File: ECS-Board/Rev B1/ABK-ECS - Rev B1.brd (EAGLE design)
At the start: 100 x 100 mm, 272 parts, among them J1 USB-B-S-RA, J10 FTSH-105-01-L-DV-NOPASTE, J11 22-05-7028-02, J12 RB1-125BAG1A, J2 MSTBA2, J3 22-05-7068-06, J4 22-05-7028-02, J5 22-05-7068-06, J6 22-05-7068-06, J7 22-05-7068-06, J8 22-05-7028-02, J9 FTSH-103-01-L-DV-NOPASTE, K1 G6K-2G-Y, SW1 B3FS-1015, SW2 B3FS-1015, T1 MMBT2907ALT3, T10 MMBT2222AL, T11 IRLML5103TRPBF, T12 MMBT2222AL, T13 IRLML5103TRPBF, T14 IRLML5103TRPBF, T15 IRLML5103TRPBF, T16 IRLML5103TRPBF, T17 MMBT2222AL, T18 MMBT2222AL, T19 MMBT2222AL, T2 EXMACHINA-LOGO-NAME, T20 MMBT2222AL, T3 IRLML5103TRPBF, T4 IRLML5103TRPBF, T5 IRLML5103TRPBF, T6 IRLML5103TRPBF, T7 MMBT2222AL, T8 MMBT2222AL, T9 MMBT2222AL, U1 AT24C512C-SSHM-B, U2 LPC1768FBD100, U3 LT3686HDDPBF, U4 LT3686HDDPBF, U5 CD4050BD, U6 CD4050BD, U7 DP83848JSQ/NOPB, X1 FC-135, X2 ASE-12, X3 3000, X4 ASE_50

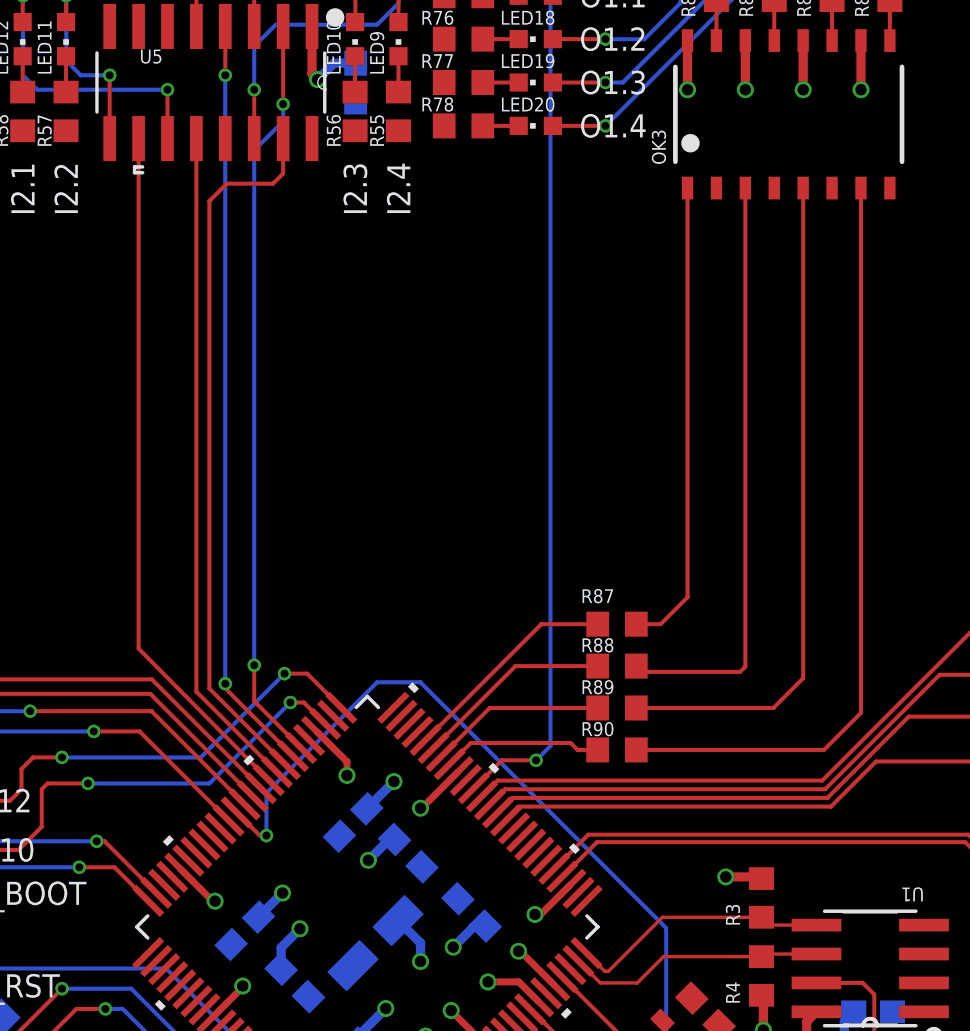
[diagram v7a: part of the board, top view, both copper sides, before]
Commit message: Remape I/O and add UART-I2C-2ADC-Encoder mcu pin
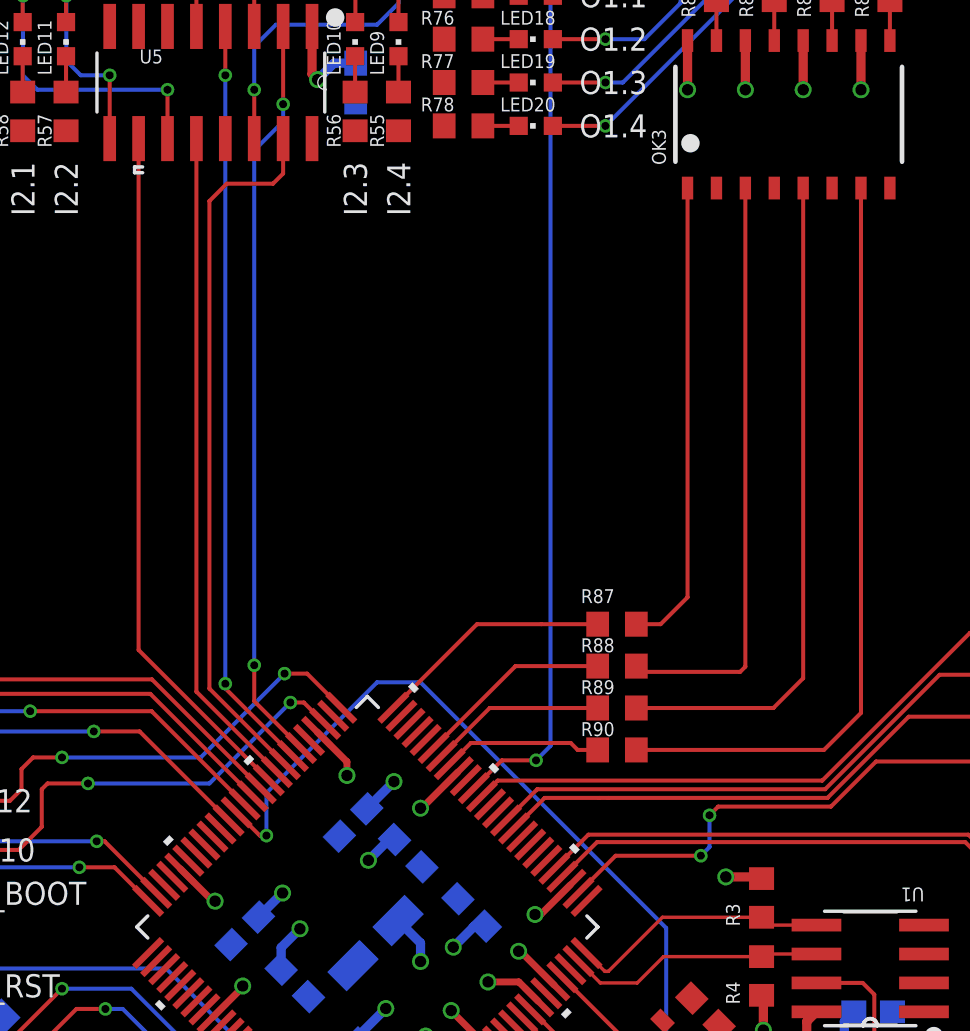
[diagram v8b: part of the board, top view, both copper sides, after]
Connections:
- new net ADC1: U2.8
- new net ADC2: U2.9
- new net ENCODER_A: U2.34
- new net ENCODER_B: U2.37
- new net ENCODER_PUSH: U2.33
- new net ENCODER_Z: U2.38
- new net I2C_SCL: U2.49
- new net I2C_SDA: U2.48
- new net UART_RX: U2.47
- new net UART_TX: U2.46
- new net USB_LED: U2.32
- net OUTPUT1.1_MCU: now also U2.50; no longer U2.46
- net OUTPUT2.2_MCU: now also U2.36; no longer U2.38
- net OUTPUT2.3_MCU: now also U2.35; no longer U2.37
- net OUTPUT2.4_MCU: now also U2.27; no longer U2.36
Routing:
- net OUTPUT2.4_MCU: track 22.9 -> 21.8 mm, vias 0 -> 2
- net OUTPUT1.1_MCU: track 9.67 -> 10.5 mm
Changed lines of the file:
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@@
 </signal>
 <signal name="OUTPUT2.4_MCU">
-<contactref element="U2" pad="36"/>
 <contactref element="R121" pad="2"/>
-<wire x1="43.766715625" y1="38.381353125" x2="44.3743625" y2="38.989" width="0.1778" layer="1"/>
-<wire x1="44.3743625" y1="38.989" x2="58.039" y2="38.989" width="0.1778" layer="1"/>
+<wire x1="53.086" y1="38.989" x2="58.039" y2="38.989" width="0.1778" layer="1"/>
 <wire x1="58.039" y1="38.989" x2="60.02" y2="40.97" width="0.1778" layer="1"/>
 <wire x1="60.02" y1="40.97" x2="65.571" y2="40.97" width="0.1778" layer="1"/>
+<contactref element="U2" pad="27"/>
+<wire x1="53.086" y1="38.989" x2="52.705" y2="38.608" width="0.1778" layer="1"/>
+<via x="52.705" y="38.608" extent="1-16" drill="0.35"/>
+<wire x1="52.705" y1="38.608" x2="52.705" y2="37.211" width="0.1778" layer="16"/>
+<wire x1="52.705" y1="37.211" x2="52.324" y2="36.83" width="0.1778" layer="16"/>
+<via x="52.324" y="36.83" extent="1-16" drill="0.35"/>
+<wire x1="52.324" y1="36.83" x2="48.579325" y2="36.83" width="0.1778" layer="1"/>
+<wire x1="48.579325" y1="36.83" x2="46.948696875" y2="35.199371875" width="0.1778" layer="1"/>
 </signal>
 <signal name="OUTPUT2.3_MCU">
-<contactref element="U2" pad="37"/>
 <contactref element="R120" pad="2"/>
-<wire x1="43.4131625" y1="38.73490625" x2="44.04825625" y2="39.37" width="0.1778" layer="1"/>
-<wire x1="44.04825625" y1="39.37" x2="57.887" y2="39.37" width="0.1778" layer="1"/>
+<wire x1="47.85825625" y1="39.37" x2="48.26" y2="39.37" width="0.1778" layer="1"/>
+<wire x1="48.26" y1="39.37" x2="57.887" y2="39.37" width="0.1778" layer="1"/>
 <wire x1="61.4555" y1="42.9385" x2="65.571" y2="42.9385" width="0.1778" layer="1"/>
 <wire x1="57.887" y1="39.37" x2="61.4555" y2="42.9385" width="0.1778" layer="1"/>
+<contactref element="U2" pad="35"/>
+<wire x1="44.12026875" y1="38.027796875" x2="45.462471875" y2="39.37" width="0.1778" layer="1"/>
+<wire x1="45.462471875" y1="39.37" x2="47.85825625" y2="39.37" width="0.1778" layer="1"/>
 </signal>
 <signal name="OUTPUT2.2_MCU">
-<contactref element="U2" pad="38"/>
 <contactref element="R119" pad="2"/>
-<wire x1="43.059609375" y1="39.088459375" x2="43.72215" y2="39.751" width="0.1778" layer="1"/>
-<wire x1="43.72215" y1="39.751" x2="57.785" y2="39.751" width="0.1778" layer="1"/>
+<wire x1="45.1363625" y1="39.751" x2="57.785" y2="39.751" width="0.1778" layer="1"/>
 <wire x1="57.785" y1="39.751" x2="62.814" y2="44.78" width="0.1778" layer="1"/>
 <wire x1="62.814" y1="44.78" x2="65.571" y2="44.78" width="0.1778" layer="1"/>
+<contactref element="U2" pad="36"/>
+<wire x1="43.766715625" y1="38.381353125" x2="45.1363625" y2="39.751" width="0.1778" layer="1"/>
 </signal>
 <signal name="N$41">
@@
 <contactref element="U2" pad="60"/>
 <contactref element="U5" pad="10"/>
-<wire x1="27.6225" y1="68.3362" x2="27.6225" y2="45.93158125" width="0.1778" layer="1"/>
-<wire x1="27.6225" y1="45.93158125" x2="33.3439625" y2="40.14911875" width="0.1778" layer="1"/>
+<wire x1="27.6225" y1="68.3362" x2="27.6225" y2="45.87058125" width="0.1778" layer="1"/>
+<wire x1="27.6225" y1="45.87058125" x2="33.3439625" y2="40.14911875" width="0.1778" layer="1"/>
 </signal>
 <signal name="VREFP">
@@
 <signal name="OUTPUT1.1_MCU">
 <contactref element="R87" pad="2"/>
-<contactref element="U2" pad="46"/>
-<wire x1="40.23118125" y1="41.916884375" x2="45.316796875" y2="47.0025" width="0.1778" layer="1"/>
-<wire x1="45.316796875" y1="47.0025" x2="47.791" y2="47.0025" width="0.1778" layer="1"/>
+<wire x1="45.316796875" y1="47.0025" x2="45.72" y2="47.0025" width="0.1778" layer="1"/>
+<contactref element="U2" pad="50"/>
+<wire x1="45.72" y1="47.0025" x2="47.791" y2="47.0025" width="0.1778" layer="1"/>
+<wire x1="38.81696875" y1="43.3311" x2="42.48836875" y2="47.0025" width="0.1778" layer="1"/>
+<wire x1="42.48836875" y1="47.0025" x2="45.316796875" y2="47.0025" width="0.1778" layer="1"/>
 </signal>
 <signal name="N$81">
@@
 <wire x1="35.939209375" y1="9.906959375" x2="51.689209375" y2="9.906959375" width="0.4064" layer="15"/>
 </signal>
+<signal name="ADC2">
+<contactref element="U2" pad="9"/>
+</signal>
+<signal name="ADC1">
+<contactref element="U2" pad="8"/>
+</signal>
+<signal name="UART_TX">
+<contactref element="U2" pad="46"/>
+</signal>
+<signal name="UART_RX">
+<contactref element="U2" pad="47"/>
+</signal>
+<signal name="I2C_SDA">
+<contactref element="U2" pad="48"/>
+</signal>
+<signal name="I2C_SCL">
+<contactref element="U2" pad="49"/>
+</signal>
+<signal name="USB_LED">
+<contactref element="U2" pad="32"/>
+</signal>
+<signal name="ENCODER_A">
+<contactref element="U2" pad="34"/>
+</signal>
+<signal name="ENCODER_B">
+<contactref element="U2" pad="37"/>
+</signal>
+<signal name="ENCODER_Z">
+<contactref element="U2" pad="38"/>
+</signal>
+<signal name="ENCODER_PUSH">
+<contactref element="U2" pad="33"/>
+</signal>
 </signals>
